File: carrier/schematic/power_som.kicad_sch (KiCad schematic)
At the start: 17 parts, among them U21004 TPS54302DDCR

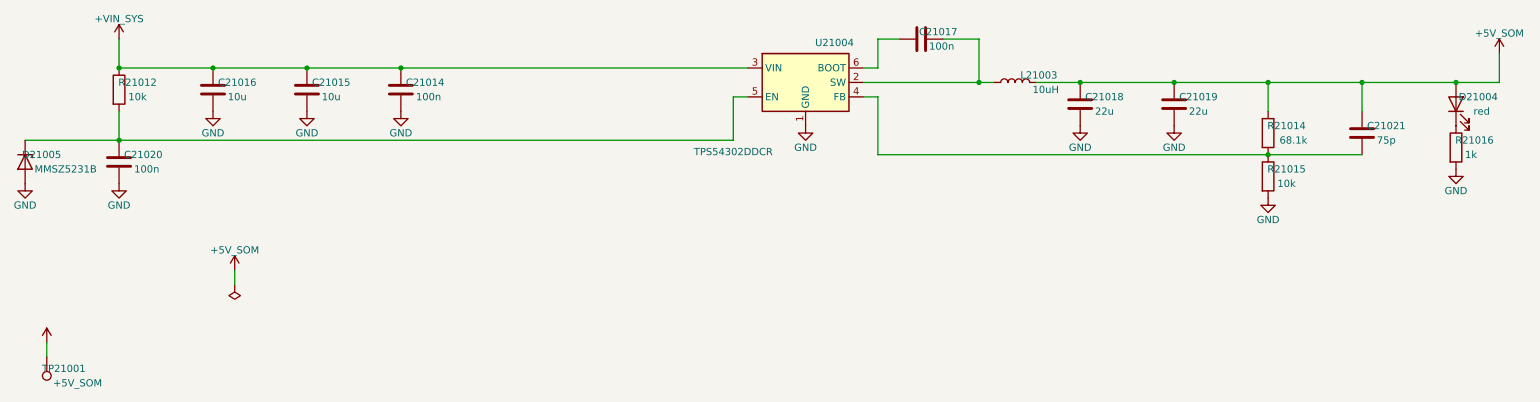
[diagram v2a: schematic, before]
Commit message: feat: USB-JTAG/UART debug bridge (CH347T) + Pmod expansion (Stream C)
Two new feature sheets (board 30 -> 33):
- usb_jtag + usb_jtag_connector: a self-powered, isolated USB-JTAG/UART debug
  bridge. CH347T (chosen over FT2232H, whose 64-pin LQFP the placer cannot route)
  on its own USB-powered island (AP2112K-3.3 LDO, USBLC6 ESD, 8MHz xtal); JTAG
  isolated to the Zynq via an SN74LVC125 buffer with default-Hi-Z OE (100k pull +
  DIP) so the existing debug_boot header owns JTAG by default (zero contention,
  netlist-proven: ZYNQ_JTAG touches only the buffer). Can program a dead board.
- pmod_expansion: a Digilent Pmod (2x6, 3.3V) — 8 IO on verified-free bank-13 PL
  pins (via FUNCTION_MAP) + a manually-gated rail + TPD4E1U06 ESD.

Pin alloc verified free (XDC 146 -> 156, no double-claims). Regression green:
board 33 sheets, selftest 59/59, pytest 219. usb_jtag render inspected (LAW 1).

Co-Authored-By: Claude Opus 4.8 <noreply@anthropic.com>
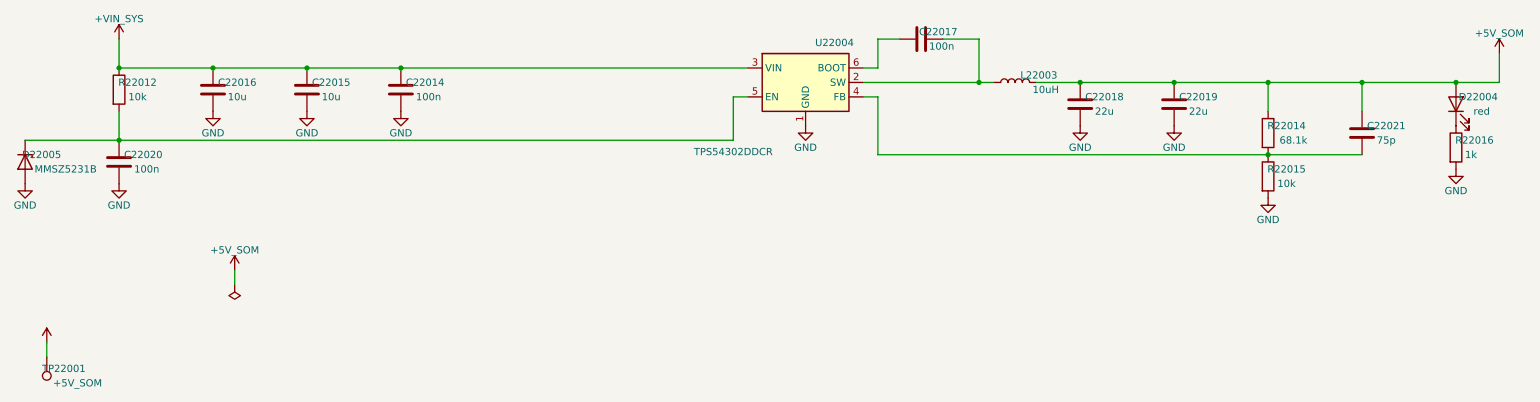
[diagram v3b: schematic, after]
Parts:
- renumbered C21014 to C22014, C21015 to C22015, C21016 to C22016, C21017 to C22017, C21018 to C22018, C21019 to C22019, C21020 to C22020, C21021 to C22021, D21004 to D22004, D21005 to D22005, L21003 to L22003, R21012 to R22012, R21014 to R22014, R21015 to R22015, R21016 to R22016, TP21001 to TP22001, U21004 to U22004
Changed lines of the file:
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@@
 		(property
 			"Reference"
-			"U21004"
+			"U22004"
 			(at 160.02 73.025 0)
 			(effects
@@
 				(path
 					"/c2797150-7a6e-556a-82f5-fdda13c31368/756f5dd1-c069-57c6-80c5-4da28b8ee2f6"
-					(reference "U21004")
+					(reference "U22004")
 					(unit 1)
 				)
@@
 		(property
 			"Reference"
-			"C21014"
+			"C22014"
 			(at 88.082 80.01 0)
 			(effects
@@
 				(path
 					"/c2797150-7a6e-556a-82f5-fdda13c31368/756f5dd1-c069-57c6-80c5-4da28b8ee2f6"
-					(reference "C21014")
+					(reference "C22014")
 					(unit 1)
 				)
@@
 		(property
 			"Reference"
-			"C21015"
+			"C22015"
 			(at 71.572 80.01 0)
 			(effects
@@
 				(path
 					"/c2797150-7a6e-556a-82f5-fdda13c31368/756f5dd1-c069-57c6-80c5-4da28b8ee2f6"
-					(reference "C21015")
+					(reference "C22015")
 					(unit 1)
 				)
@@
 		(property
 			"Reference"
-			"C21016"
+			"C22016"
 			(at 55.062 80.01 0)
 			(effects
@@
 				(path
 					"/c2797150-7a6e-556a-82f5-fdda13c31368/756f5dd1-c069-57c6-80c5-4da28b8ee2f6"
-					(reference "C21016")
+					(reference "C22016")
 					(unit 1)
 				)
@@
 		(property
 			"Reference"
-			"R21012"
+			"R22012"
 			(at 37.536 80.01 0)
 			(effects
@@
 				(path
 					"/c2797150-7a6e-556a-82f5-fdda13c31368/756f5dd1-c069-57c6-80c5-4da28b8ee2f6"
-					(reference "R21012")
+					(reference "R22012")
 					(unit 1)
 				)
@@
 		(property
 			"Reference"
-			"C21020"
+			"C22020"
 			(at 38.552 92.71 0)
 			(effects
@@
 				(path
 					"/c2797150-7a6e-556a-82f5-fdda13c31368/756f5dd1-c069-57c6-80c5-4da28b8ee2f6"
-					(reference "C21020")
+					(reference "C22020")
 					(unit 1)
 				)
@@
 		(property
 			"Reference"
-			"D21005"
+			"D22005"
 			(at 20.677 92.71 90)
 			(effects
@@
 				(path
 					"/c2797150-7a6e-556a-82f5-fdda13c31368/756f5dd1-c069-57c6-80c5-4da28b8ee2f6"
-					(reference "D21005")
+					(reference "D22005")
 					(unit 1)
 				)
@@
 		(property
 			"Reference"
-			"C21017"
+			"C22017"
 			(at 178.252 71.12 90)
 			(effects
@@
 				(path
 					"/c2797150-7a6e-556a-82f5-fdda13c31368/756f5dd1-c069-57c6-80c5-4da28b8ee2f6"
-					(reference "C21017")
+					(reference "C22017")
 					(unit 1)
 				)
@@
 		(property
 			"Reference"
-			"L21003"
+			"L22003"
 			(at 195.936 78.74 90)
 			(effects
@@
 				(path
 					"/c2797150-7a6e-556a-82f5-fdda13c31368/756f5dd1-c069-57c6-80c5-4da28b8ee2f6"
-					(reference "L21003")
+					(reference "L22003")
 					(unit 1)
 				)
@@
 		(property
 			"Reference"
-			"C21018"
+			"C22018"
 			(at 207.462 82.55 0)
 			(effects
@@
 				(path
 					"/c2797150-7a6e-556a-82f5-fdda13c31368/756f5dd1-c069-57c6-80c5-4da28b8ee2f6"
-					(reference "C21018")
+					(reference "C22018")
 					(unit 1)
 				)
@@
 		(property
 			"Reference"
-			"C21019"
+			"C22019"
 			(at 223.972 82.55 0)
 			(effects
@@
 				(path
 					"/c2797150-7a6e-556a-82f5-fdda13c31368/756f5dd1-c069-57c6-80c5-4da28b8ee2f6"
-					(reference "C21019")
+					(reference "C22019")
 					(unit 1)
 				)
@@
 		(property
 			"Reference"
-			"R21014"
+			"R22014"
 			(at 239.466 87.63 0)
 			(effects
@@
 				(path
 					"/c2797150-7a6e-556a-82f5-fdda13c31368/756f5dd1-c069-57c6-80c5-4da28b8ee2f6"
-					(reference "R21014")
+					(reference "R22014")
 					(unit 1)
 				)
@@
 		(property
 			"Reference"
-			"R21015"
+			"R22015"
 			(at 239.466 95.25 0)
 			(effects
@@
 				(path
 					"/c2797150-7a6e-556a-82f5-fdda13c31368/756f5dd1-c069-57c6-80c5-4da28b8ee2f6"
-					(reference "R21015")
+					(reference "R22015")
 					(unit 1)
 				)
@@
 		(property
 			"Reference"
-			"C21021"
+			"C22021"
 			(at 256.992 87.63 0)
 			(effects
@@
 				(path
 					"/c2797150-7a6e-556a-82f5-fdda13c31368/756f5dd1-c069-57c6-80c5-4da28b8ee2f6"
-					(reference "C21021")
+					(reference "C22021")
 					(unit 1)
 				)
@@
 		(property
 			"Reference"
-			"D21004"
+			"D22004"
 			(at 273.153 82.55 90)
 			(effects
@@
 				(path
 					"/c2797150-7a6e-556a-82f5-fdda13c31368/756f5dd1-c069-57c6-80c5-4da28b8ee2f6"
-					(reference "D21004")
+					(reference "D22004")
 					(unit 1)
 				)
@@
 		(property
 			"Reference"
-			"R21016"
+			"R22016"
 			(at 272.486 90.17 0)
 			(effects
@@
 				(path
 					"/c2797150-7a6e-556a-82f5-fdda13c31368/756f5dd1-c069-57c6-80c5-4da28b8ee2f6"
-					(reference "R21016")
+					(reference "R22016")
 					(unit 1)
 				)
@@
 		(property
 			"Reference"
-			"TP21001"
+			"TP22001"
 			(at 24.582 130.302 0)
 			(effects
@@
 				(path
 					"/c2797150-7a6e-556a-82f5-fdda13c31368/756f5dd1-c069-57c6-80c5-4da28b8ee2f6"
-					(reference "TP21001")
+					(reference "TP22001")
 					(unit 1)
 				)
@@
 		(property
 			"Reference"
-			"#PWR21001"
+			"#PWR22001"
 			(at 34.29 69.85 0)
 			(effects
@@
 				(path
 					"/c2797150-7a6e-556a-82f5-fdda13c31368/756f5dd1-c069-57c6-80c5-4da28b8ee2f6"
-					(reference "#PWR21001")
+					(reference "#PWR22001")
 					(unit 1)
 				)
@@
 		(property
 			"Reference"
-			"#PWR21002"
+			"#PWR22002"
 			(at 83.82 82.55 0)
 			(effects
@@
 				(path
 					"/c2797150-7a6e-556a-82f5-fdda13c31368/756f5dd1-c069-57c6-80c5-4da28b8ee2f6"
-					(reference "#PWR21002")
+					(reference "#PWR22002")
 					(unit 1)
 				)
@@
 		(property
 			"Reference"
-			"#PWR21003"
+			"#PWR22003"
 			(at 67.31 82.55 0)
 			(effects
@@
 				(path
 					"/c2797150-7a6e-556a-82f5-fdda13c31368/756f5dd1-c069-57c6-80c5-4da28b8ee2f6"
-					(reference "#PWR21003")
+					(reference "#PWR22003")
 					(unit 1)
 				)
@@
 		(property
 			"Reference"
-			"#PWR21004"
+			"#PWR22004"
 			(at 50.8 82.55 0)
 			(effects
@@
 				(path
 					"/c2797150-7a6e-556a-82f5-fdda13c31368/756f5dd1-c069-57c6-80c5-4da28b8ee2f6"
-					(reference "#PWR21004")
+					(reference "#PWR22004")
 					(unit 1)
 				)
@@
 		(property
 			"Reference"
-			"#PWR21005"
+			"#PWR22005"
 			(at 34.29 95.25 0)
 			(effects
@@
 				(path
 					"/c2797150-7a6e-556a-82f5-fdda13c31368/756f5dd1-c069-57c6-80c5-4da28b8ee2f6"
-					(reference "#PWR21005")
+					(reference "#PWR22005")
 					(unit 1)
 				)
@@
 		(property
 			"Reference"
-			"#PWR21006"
+			"#PWR22006"
 			(at 17.78 95.25 0)
 			(effects
@@
 				(path
 					"/c2797150-7a6e-556a-82f5-fdda13c31368/756f5dd1-c069-57c6-80c5-4da28b8ee2f6"
-					(reference "#PWR21006")
+					(reference "#PWR22006")
 					(unit 1)
 				)
@@
 		(property
 			"Reference"
-			"#PWR21007"
+			"#PWR22007"
 			(at 154.94 85.09 0)
 			(effects
@@
 				(path
 					"/c2797150-7a6e-556a-82f5-fdda13c31368/756f5dd1-c069-57c6-80c5-4da28b8ee2f6"
-					(reference "#PWR21007")
+					(reference "#PWR22007")
 					(unit 1)
 				)
@@
 		(property
 			"Reference"
-			"#PWR21008"
+			"#PWR22008"
 			(at 203.2 85.09 0)
 			(effects
@@
 				(path
 					"/c2797150-7a6e-556a-82f5-fdda13c31368/756f5dd1-c069-57c6-80c5-4da28b8ee2f6"
-					(reference "#PWR21008")
+					(reference "#PWR22008")
 					(unit 1)
 				)
@@
 		(property
 			"Reference"
-			"#PWR21009"
+			"#PWR22009"
 			(at 219.71 85.09 0)
 			(effects
@@
 				(path
 					"/c2797150-7a6e-556a-82f5-fdda13c31368/756f5dd1-c069-57c6-80c5-4da28b8ee2f6"
-					(reference "#PWR21009")
+					(reference "#PWR22009")
 					(unit 1)
 				)
@@
 		(property
 			"Reference"
-			"#PWR21010"
+			"#PWR22010"
 			(at 236.22 97.79 0)
 			(effects
@@
 				(path
 					"/c2797150-7a6e-556a-82f5-fdda13c31368/756f5dd1-c069-57c6-80c5-4da28b8ee2f6"
-					(reference "#PWR21010")
+					(reference "#PWR22010")
 					(unit 1)
 				)
@@
 		(property
 			"Reference"
-			"#PWR21011"
+			"#PWR22011"
 			(at 269.24 92.71 0)
 			(effects
@@
 				(path
 					"/c2797150-7a6e-556a-82f5-fdda13c31368/756f5dd1-c069-57c6-80c5-4da28b8ee2f6"
-					(reference "#PWR21011")
+					(reference "#PWR22011")
 					(unit 1)
 				)
@@
 		(property
 			"Reference"
-			"#PWR21012"
+			"#PWR22012"
 			(at 276.86 72.39 0)
 			(effects
@@
 				(path
 					"/c2797150-7a6e-556a-82f5-fdda13c31368/756f5dd1-c069-57c6-80c5-4da28b8ee2f6"
-					(reference "#PWR21012")
+					(reference "#PWR22012")
 					(unit 1)
 				)
@@
 		(property
 			"Reference"
-			"#PWR21015"
+			"#PWR22015"
 			(at 54.61 110.49 0)
 			(effects
@@
 				(path
 					"/c2797150-7a6e-556a-82f5-fdda13c31368/756f5dd1-c069-57c6-80c5-4da28b8ee2f6"
-					(reference "#PWR21015")
+					(reference "#PWR22015")
 					(unit 1)
 				)
@@
 		(property
 			"Reference"
-			"#FLG21003"
+			"#FLG22003"
 			(at 54.61 113.03 0)
 			(effects
@@
 				(path
 					"/c2797150-7a6e-556a-82f5-fdda13c31368/756f5dd1-c069-57c6-80c5-4da28b8ee2f6"
-					(reference "#FLG21003")
+					(reference "#FLG22003")
 					(unit 1)
 				)
@@
 		(property
 			"Reference"
-			"#PWR21016"
+			"#PWR22016"
 			(at 21.59 123.19 0)
 			(effects
@@
 				(path
 					"/c2797150-7a6e-556a-82f5-fdda13c31368/756f5dd1-c069-57c6-80c5-4da28b8ee2f6"
-					(reference "#PWR21016")
-					(unit 1)
-				)
+					(reference "#PWR22016")
+					(unit 1)
+				)

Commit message: bom: sourcing risk+cost report + C1591->C14663 (Extended->Basic 100n)
Stream F — live JLCPCB/LCSC sourcing pass over all 95 distinct BOM parts.

Report: carrier/manufacturing/SOURCING.md — per-part stock / Basic-vs-Extended
/ unit price / risk + flagged second sources, and a rollup (94 parts post-swap,
64 Extended of which 2 Preferred -> 62 feeder fees = ~$186, 15 parts <5k stock,
6 procurement-critical <300). Data from the JLCPCB parts API (live).

Applied swap (only clean Basic drop-in on the board): 100 nF 0603 decoupling
C1591 (Samsung CL10B104KB8NNNC, Extended, 2.08M) -> C14663 (YAGEO
CC0603KRX7R9BB104, Basic, 17.8M). IDENTICAL 100nF/50V/X7R/+-10%/0603, same
footprint+symbol -> netlist & render byte-identical; ratings.py already carries
C14663 with matching ratings. Merges 71 Extended + 12 existing-Basic positions
onto one 83-piece Basic line: removes one Extended feeder fee, cheaper unit,
8.5x more stock.

Everything else is REPORT-ONLY: every other Extended part is
Extended-by-necessity (no JLC-Basic equivalent — precise E96 values, specialty
ICs/connectors) or has only a footprint-mismatched / MPN-ambiguous alternate.
Also flagged (not fixed): C25750 ("40.2k" power:R1) currently resolves on LCSC
to a 120k 0402 part — a data-integrity bug; recommend C12447 after intent check.

Gates: part-rules PASS (132 checks, 0 findings); board PASS (33 sheets, golden
renders 33/33 match, DRC 0); selftest 59/59; m1_rc PASS; pytest 219 passed.
BOM regen deterministic (md5 stable).

Co-Authored-By: Claude Opus 4.8 <noreply@anthropic.com>
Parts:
- C22014, C22017, C22020: LCSC C1591 -> C14663
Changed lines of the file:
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@@
 		(property
 			"LCSC"
-			"C1591"
+			"C14663"
 			(at 83.82 81.28 0)
 			(effects
@@
 		(property
 			"LCSC"
-			"C1591"
+			"C14663"
 			(at 34.29 93.98 0)
 			(effects
@@
 		(property
 			"LCSC"
-			"C1591"
+			"C14663"
 			(at 175.26 72.39 0)
 			(effects
